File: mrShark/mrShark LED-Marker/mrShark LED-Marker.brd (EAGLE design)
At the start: 26 x 31 mm, 38 parts, among them CON1 DF12-20DS, IC1 PCA9552PW

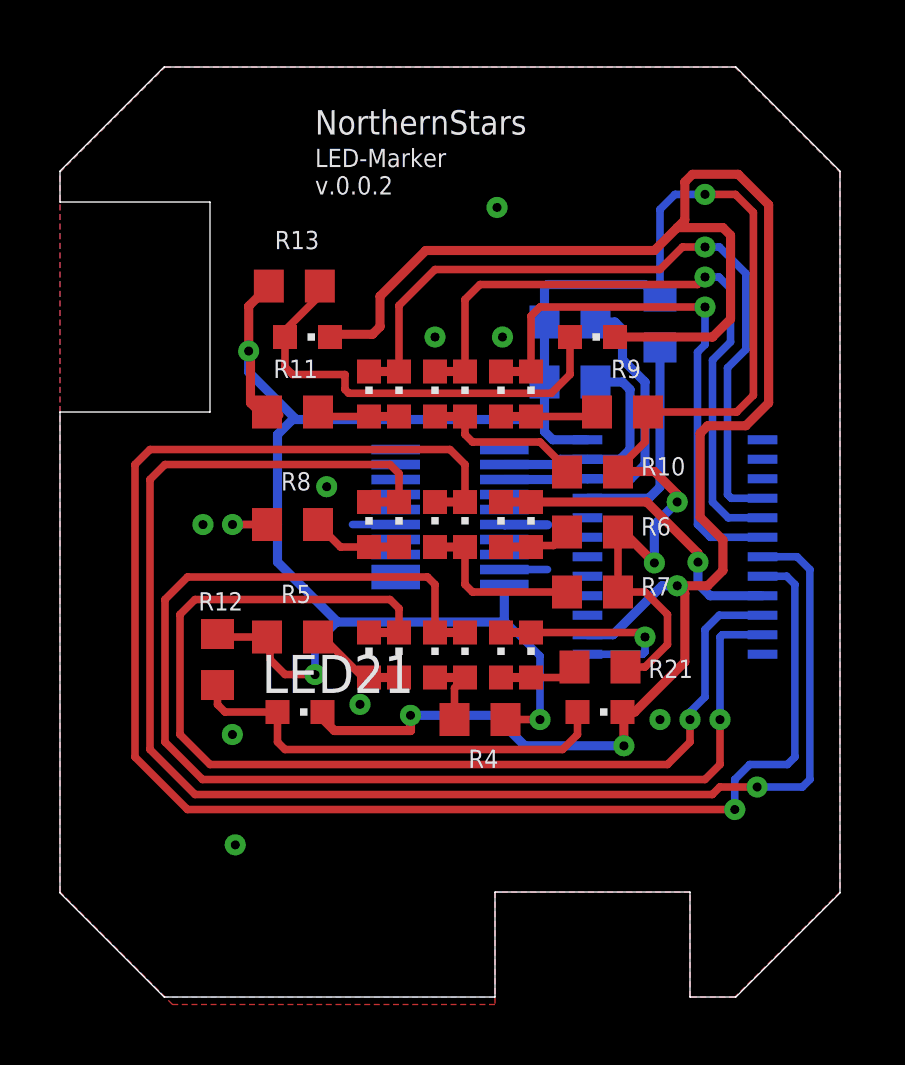
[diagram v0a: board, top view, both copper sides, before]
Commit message: Updated mrShark 1.2 & 1.3 Updated mrShark Adapter Updated mrShark LED-Marker to version 0.0.3
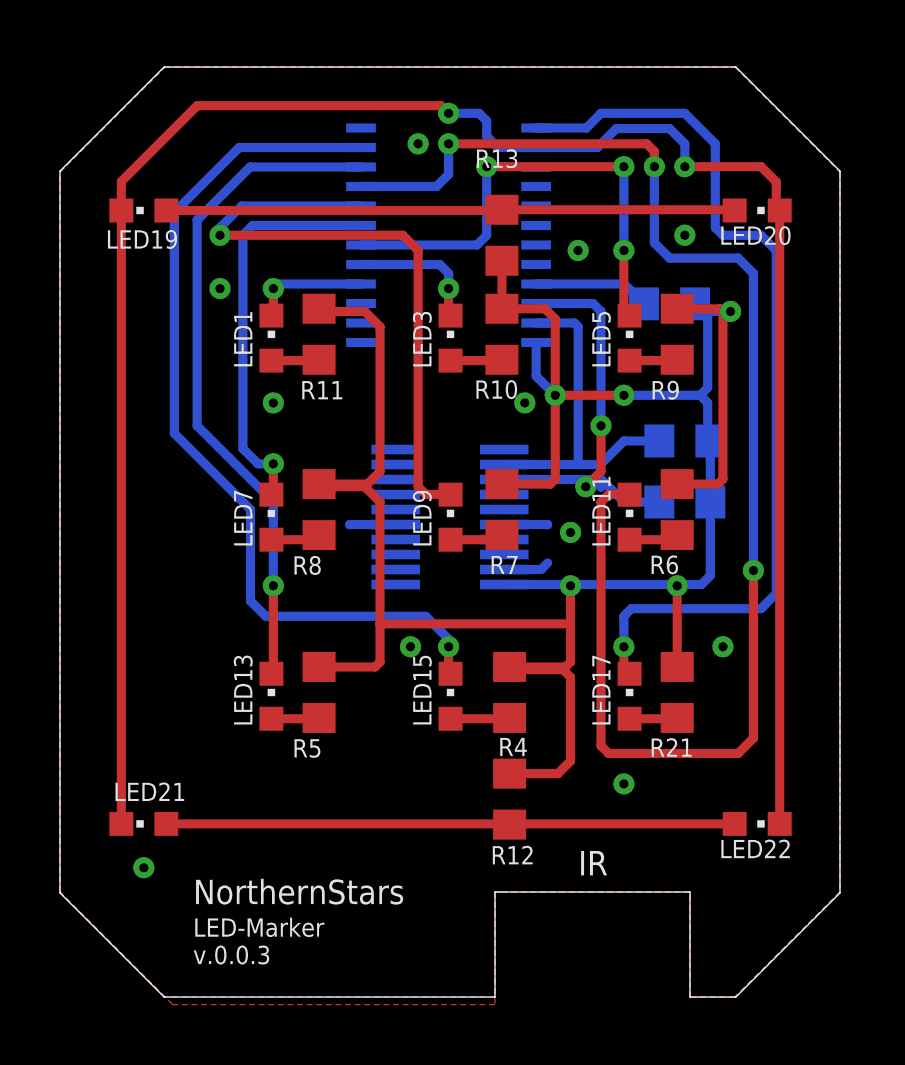
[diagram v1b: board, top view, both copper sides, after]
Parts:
- removed LED10, LED12, LED14, LED16, LED18, LED4, LED6, LED8: (no value), led:CHIPLED_0603
- removed LED2: LW L283, led:CHIPLED_0603
- moved IC1 12.8 mm to (13.0, 24.9), turned to 90 degrees
- moved R12 10.8 mm to (15.0, 6.10)
- moved R13 7.12 mm to (14.7, 24.9), turned to 90 degrees
- moved R3 7.12 mm to (20.8, 16.0), turned to 180 degrees
- moved LED20 6.92 mm to (23.2, 25.7)
- moved LED19 6.90 mm to (2.79, 25.7), turned to 90 degrees
- moved LED22 6.43 mm to (23.2, 5.27)
- moved LED21 6.40 mm to (2.79, 5.27), turned to 90 degrees
- moved R10 5.49 mm to (14.7, 21.6), turned to 270 degrees
- moved LED5 4.67 mm to (19.0, 21.5)
- moved LED17 4.50 mm to (19.0, 9.53)
- moved R2 4.30 mm to (20.8, 18.0), turned to 180 degrees
- moved LED11 4.29 mm to (19.0, 15.5)
- moved R7 4.08 mm to (14.7, 15.7), turned to 270 degrees
- moved LED1 3.75 mm to (7.05, 21.5)
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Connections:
- net N$10: no longer LED6.A
- net N$11: no longer LED4.A
- net N$12: no longer LED2.A
- net N$13: no longer LED2.C
- net N$14: no longer LED4.C
- net N$15: no longer LED6.C
- net N$16: no longer LED8.C
- net N$17: no longer LED10.C
- net N$18: no longer LED12.C
- net N$19: no longer LED14.C
- net N$2: no longer LED18.A
- net N$20: no longer LED16.C
- net N$21: no longer LED18.C
- net N$4: no longer LED16.A
- net N$5: no longer LED14.A
- net N$6: no longer LED12.A
- net N$7: no longer LED10.A
- net N$8: no longer LED8.A
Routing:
- net N$16: track 51.2 -> 13.5 mm
- net N$18: track 10.6 -> 47.9 mm, vias 1 -> 3
- net N$17: track 54.4 -> 21.1 mm
- net N$21: track 7.31 -> 30.6 mm
- net N$13: track 24.8 -> 3.91 mm
- net N$14: track 22.0 -> 4.48 mm
- net N$19: track 37.2 -> 22.4 mm
- net N$20: track 42.5 -> 29.4 mm
- net VCC: track 88.0 -> 83.9 mm, vias 7 -> 5
- net N$3: track 14.8 -> 19.0 mm
- net N$9: track 14.8 -> 19.0 mm
- net N$7: track 5.75 -> 1.78 mm
- net SDA: track 7.65 -> 11.5 mm
- net N$11: track 5.58 -> 1.73 mm
- net SCL: track 10.7 -> 14.4 mm, vias 0 -> 2
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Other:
- outline, holes or cut-outs redrawn
- board text added: "IR"
- board text added: "LED-Marker v.0.0.3"
- board text removed: "LED-Marker v.0.0.2"

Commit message: Updated LED Marker to version 1.0 Fixed a bug with wrong placed led and updated connection header layout.
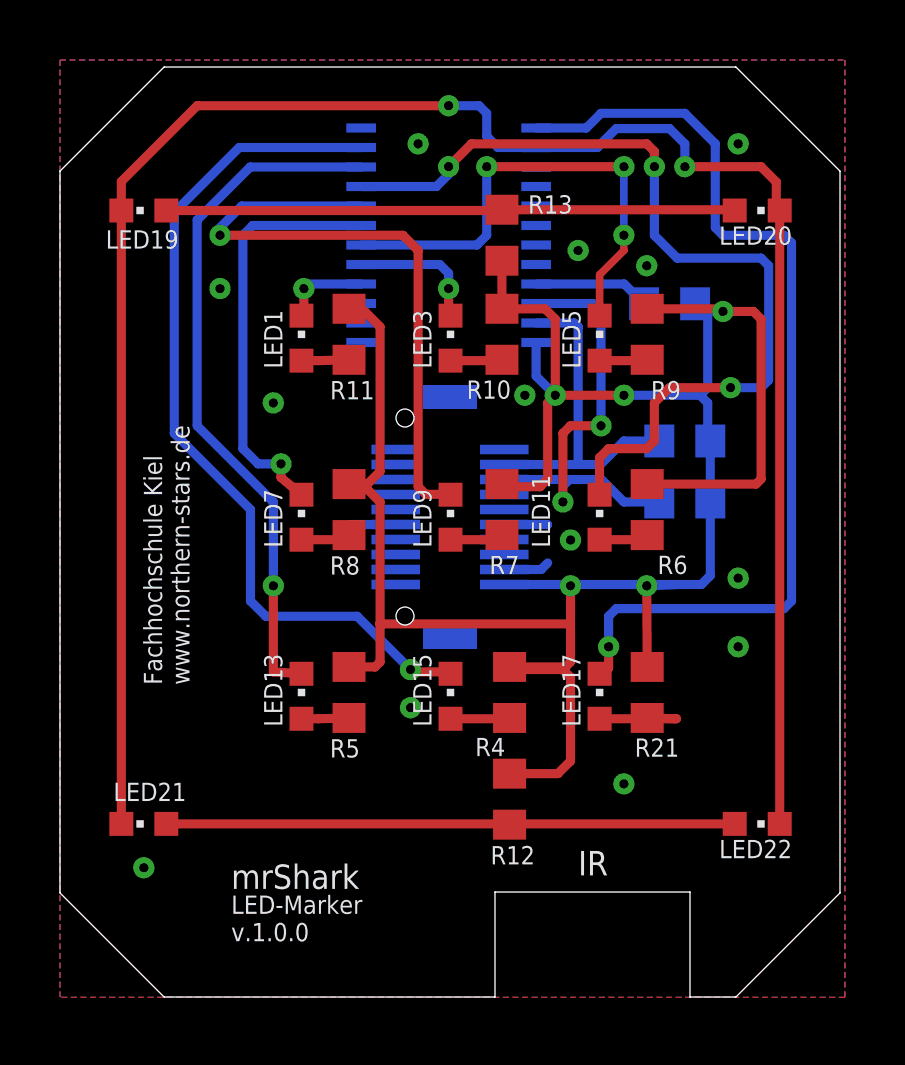
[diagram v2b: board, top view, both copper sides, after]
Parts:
- moved LED1 1.00 mm to (8.05, 21.5)
- moved LED13 1.00 mm to (8.05, 9.53)
- moved LED7 1.00 mm to (8.05, 15.5)
- moved LED11 1.00 mm to (18.0, 15.5)
- moved LED17 1.00 mm to (18.0, 9.53)
- moved LED5 1.00 mm to (18.0, 21.5)
- moved R11 1.00 mm to (9.64, 21.6)
- moved R21 1.00 mm to (19.6, 9.65)
- moved R5 1.00 mm to (9.64, 9.65)
- moved R6 1.00 mm to (19.6, 15.7)
- moved R8 1.00 mm to (9.64, 15.7)
- moved R9 1.00 mm to (19.6, 21.6)
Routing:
- net N$18: track 47.9 -> 30.1 mm
- net N$2: track 1.60 -> 3.53 mm
- net N$21: track 30.6 -> 32.5 mm
- net SCL: track 14.4 -> 16.1 mm
- net N$13: track 3.91 -> 2.91 mm
- net N$19: track 22.4 -> 23.2 mm
- net VCC: track 83.9 -> 84.6 mm
- net N$20: track 29.4 -> 28.7 mm
- net N$16: track 13.5 -> 14.0 mm
- net GND: vias 11 -> 13
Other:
- board text added: "Fachhochschule Kiel www.northern-stars.de"
- board text added: "LED-Marker v.1.0.0"
- board text added: "mrShark"
- board text removed: "LED-Marker v.0.0.3"
- board text removed: "NorthernStars"
